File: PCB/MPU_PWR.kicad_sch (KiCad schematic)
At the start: 1 part, among them U2 STM32MP157FABx

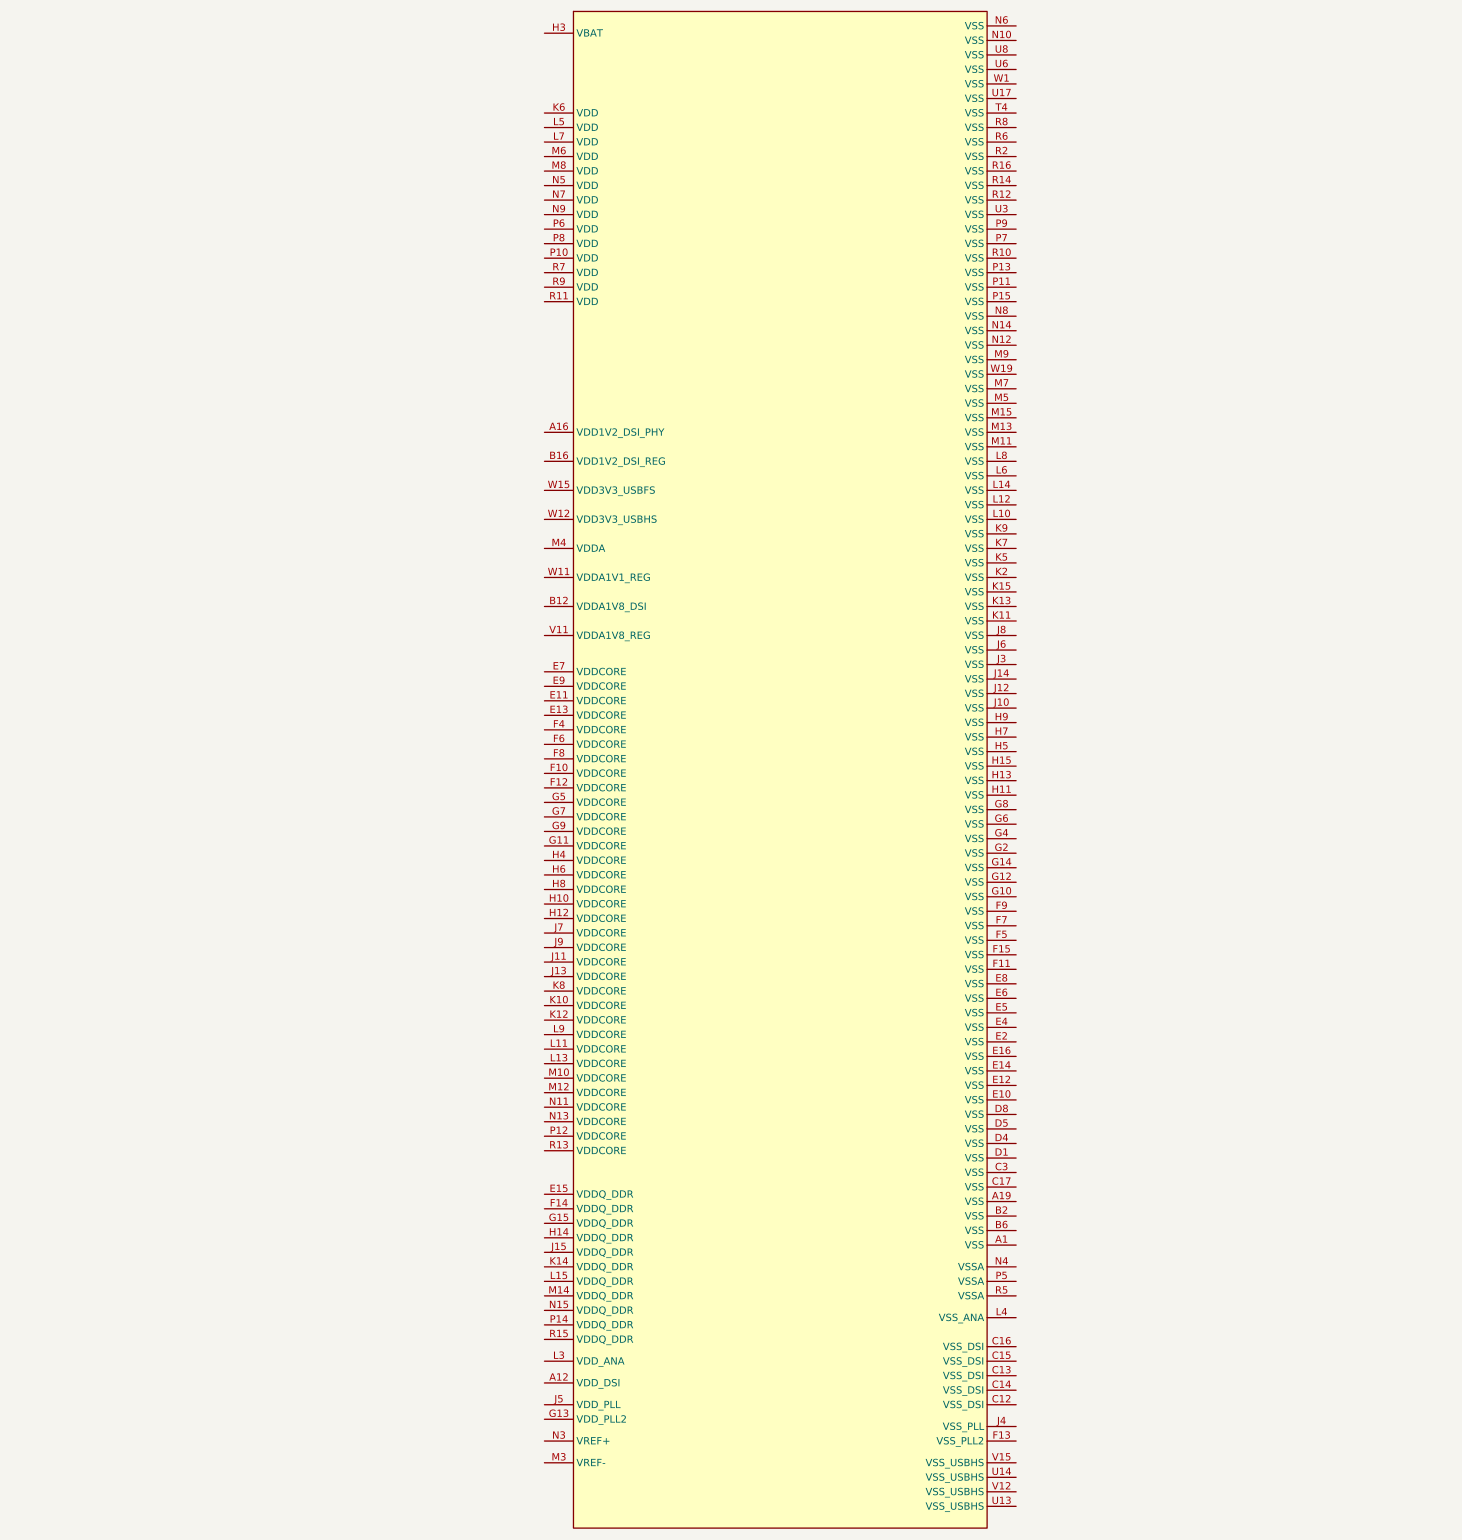
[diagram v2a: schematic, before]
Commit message: PCB_UPDATE. PWR DONE, DDR STARTED
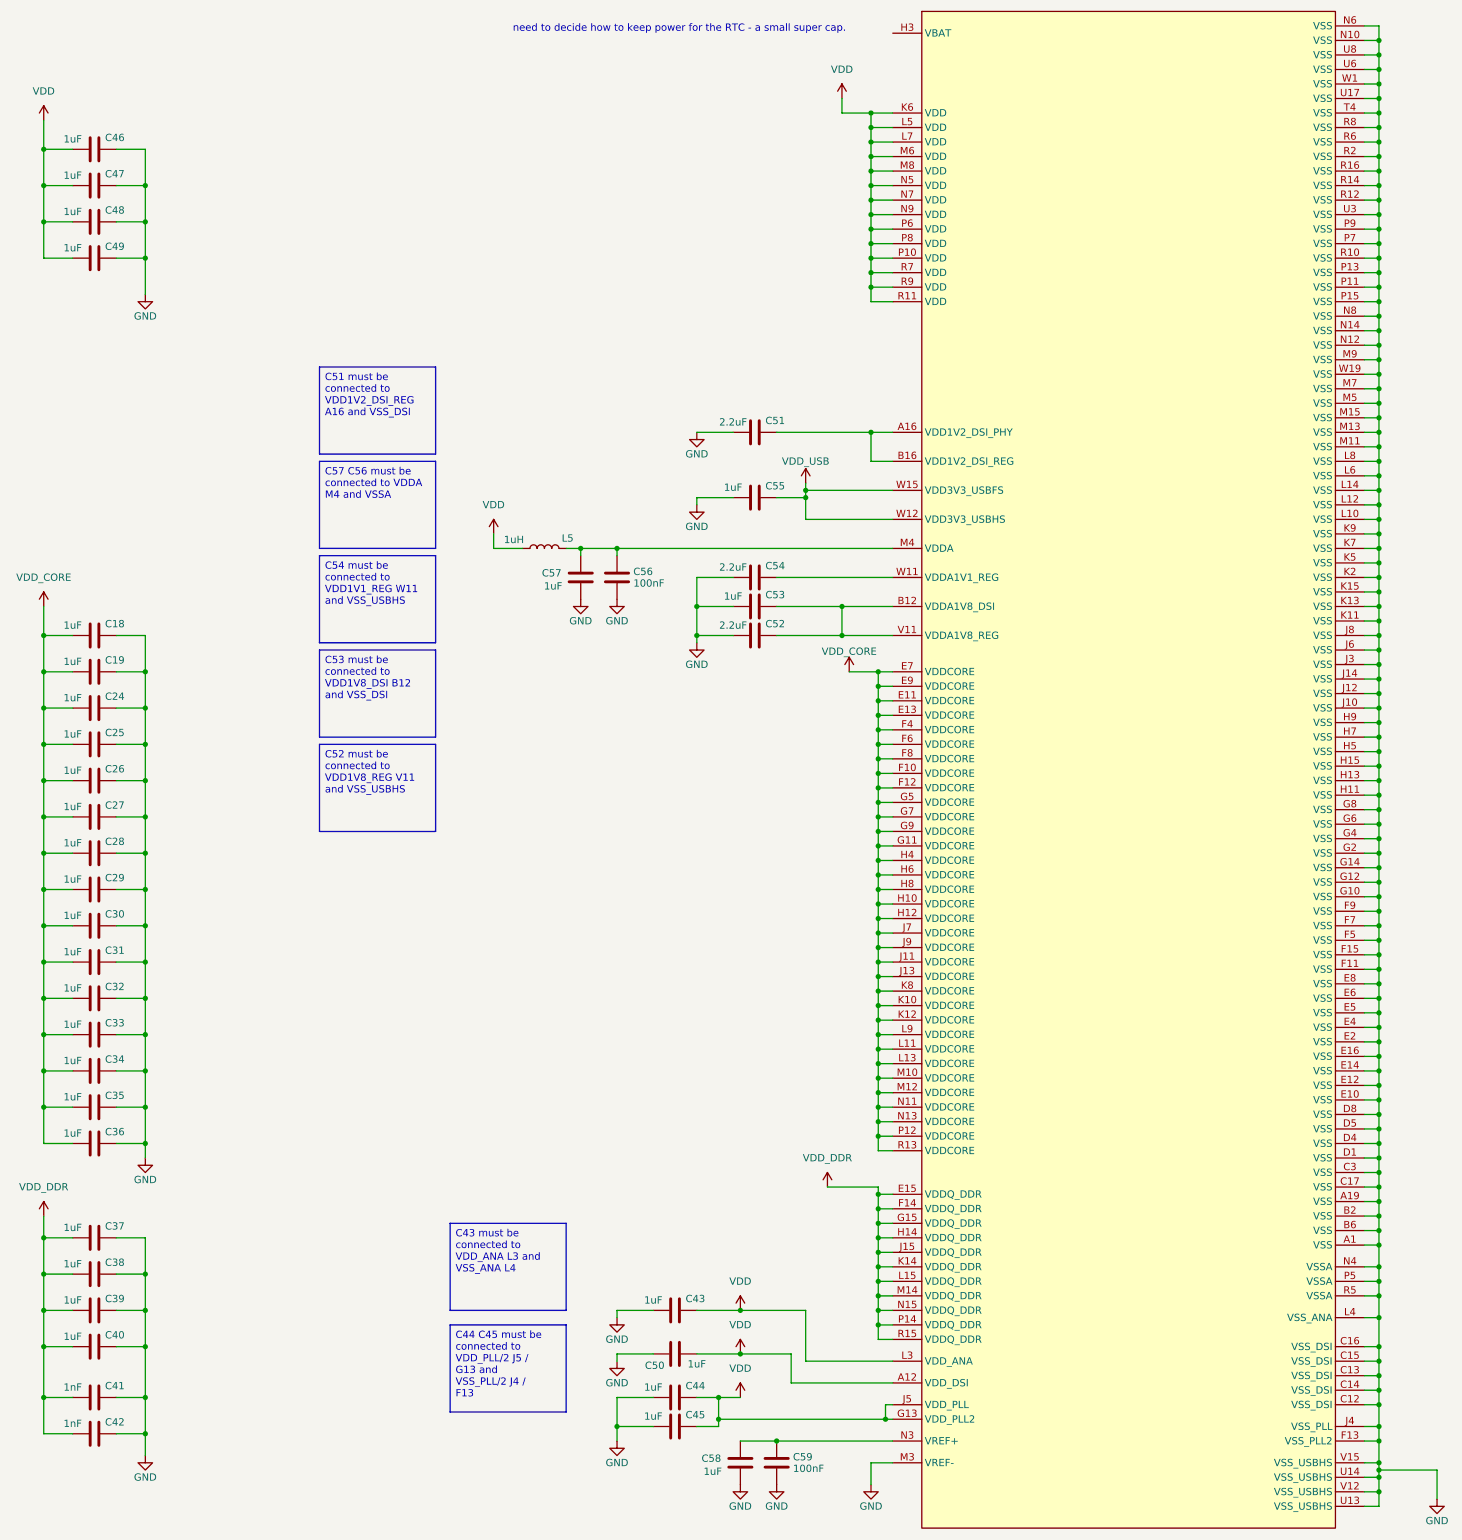
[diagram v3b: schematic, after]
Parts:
- added C18, C19, C24, C25, C26, C27, C28, C29, C30, C31, C32, C33, C34, C35, C36, C37, C38, C39, C40, C43, C44, C45, C46, C47, C48, C49, C50, C53, C55, C57, C58: 1uF, Capacitor_SMD:C_0402_1005Metric, symbol Device:C
- added C41, C42: 1nF, Capacitor_SMD:C_0402_1005Metric, symbol Device:C
- added C51, C52, C54: 2.2uF, Capacitor_SMD:C_0402_1005Metric, symbol Device:C
- added C56, C59: 100nF, Capacitor_SMD:C_0402_1005Metric, symbol Device:C
- added L5: 1uH, Inductor_SMD:L_0201_0603Metric, symbol Device:L
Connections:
- net GND: now reaches U2.A1 (VSS)
- net GND: now also U2.A19 (VSS), U2.B2 (VSS), U2.B6 (VSS), U2.C12 (VSS_DSI), U2.C13 (VSS_DSI), U2.C14 (VSS_DSI), U2.C15 (VSS_DSI), U2.C16 (VSS_DSI), U2.C17 (VSS), U2.C3 (VSS), U2.D1 (VSS), U2.D4 (VSS), U2.D5 (VSS), U2.D8 (VSS), U2.E10 (VSS), U2.E12 (VSS), U2.E14 (VSS), U2.E16 (VSS), U2.E2 (VSS), U2.E4 (VSS), U2.E5 (VSS), U2.E6 (VSS), U2.E8 (VSS), U2.F11 (VSS), U2.F13 (VSS_PLL2), U2.F15 (VSS), U2.F5 (VSS), U2.F7 (VSS), U2.F9 (VSS), U2.G10 (VSS), U2.G12 (VSS), U2.G14 (VSS), U2.G2 (VSS), U2.G4 (VSS), U2.G6 (VSS), U2.G8 (VSS), U2.H11 (VSS), U2.H13 (VSS), U2.H15 (VSS), U2.H5 (VSS), U2.H7 (VSS), U2.H9 (VSS), U2.J10 (VSS), U2.J12 (VSS), U2.J14 (VSS), U2.J3 (VSS), U2.J4 (VSS_PLL), U2.J6 (VSS), U2.J8 (VSS), U2.K11 (VSS), U2.K13 (VSS), U2.K15 (VSS), U2.K2 (VSS), U2.K5 (VSS), U2.K7 (VSS), U2.K9 (VSS), U2.L10 (VSS), U2.L12 (VSS), U2.L14 (VSS), U2.L4 (VSS_ANA), U2.L6 (VSS), U2.L8 (VSS), U2.M11 (VSS), U2.M13 (VSS), U2.M15 (VSS), U2.M3 (VREF-), U2.M5 (VSS), U2.M7 (VSS), U2.M9 (VSS), U2.N10 (VSS), U2.N12 (VSS), U2.N14 (VSS), U2.N4 (VSSA), U2.N6 (VSS), U2.N8 (VSS), U2.P11 (VSS), U2.P13 (VSS), U2.P15 (VSS), U2.P5 (VSSA), U2.P7 (VSS), U2.P9 (VSS), U2.R10 (VSS), U2.R12 (VSS), U2.R14 (VSS), U2.R16 (VSS), U2.R2 (VSS), U2.R5 (VSSA), U2.R6 (VSS), U2.R8 (VSS), U2.T4 (VSS), U2.U13 (VSS_USBHS), U2.U14 (VSS_USBHS), U2.U17 (VSS), U2.U3 (VSS), U2.U6 (VSS), U2.U8 (VSS), U2.V12 (VSS_USBHS), U2.V15 (VSS_USBHS), U2.W1 (VSS), U2.W19 (VSS), C18.1, C19.1, C24.1, C25.1, C26.1, C27.1, C28.1, C29.1, C30.1, C31.1, C32.1, C33.1, C34.1, C35.1, C36.1, C37.1, C38.1, C39.1, C40.1, C41.1, C42.1, C43.2, C44.2, C45.2, C46.1, C47.1, C48.1, C49.1, C50.1, C51.2, C52.2, C53.2, C54.2, C55.2, C56.2, C57.2, C58.2, C59.2
- net VDD: now reaches U2.A12 (VDD_DSI)
- net VDD: now also U2.G13 (VDD_PLL2), U2.J5 (VDD_PLL), U2.K6 (VDD), U2.L3 (VDD_ANA), U2.L5 (VDD), U2.L7 (VDD), U2.M6 (VDD), U2.M8 (VDD), U2.N5 (VDD), U2.N7 (VDD), U2.N9 (VDD), U2.P10 (VDD), U2.P6 (VDD), U2.P8 (VDD), U2.R11 (VDD), U2.R7 (VDD), U2.R9 (VDD), C43.1, C44.1, C45.1, C46.2, C47.2, C48.2, C49.2, C50.2, L5.1
- net at U2.A16 (VDD1V2_DSI_PHY): now also U2.B16 (VDD1V2_DSI_REG), C51.1
- net at U2.B12 (VDDA1V8_DSI): now also U2.V11 (VDDA1V8_REG), C52.1, C53.1
- net VDD_CORE: now reaches U2.E11 (VDDCORE)
- net VDD_CORE: now also U2.E13 (VDDCORE), U2.E7 (VDDCORE), U2.E9 (VDDCORE), U2.F10 (VDDCORE), U2.F12 (VDDCORE), U2.F4 (VDDCORE), U2.F6 (VDDCORE), U2.F8 (VDDCORE), U2.G11 (VDDCORE), U2.G5 (VDDCORE), U2.G7 (VDDCORE), U2.G9 (VDDCORE), U2.H10 (VDDCORE), U2.H12 (VDDCORE), U2.H4 (VDDCORE), U2.H6 (VDDCORE), U2.H8 (VDDCORE), U2.J11 (VDDCORE), U2.J13 (VDDCORE), U2.J7 (VDDCORE), U2.J9 (VDDCORE), U2.K10 (VDDCORE), U2.K12 (VDDCORE), U2.K8 (VDDCORE), U2.L11 (VDDCORE), U2.L13 (VDDCORE), U2.L9 (VDDCORE), U2.M10 (VDDCORE), U2.M12 (VDDCORE), U2.N11 (VDDCORE), U2.N13 (VDDCORE), U2.P12 (VDDCORE), U2.R13 (VDDCORE), C18.2, C19.2, C24.2, C25.2, C26.2, C27.2, C28.2, C29.2, C30.2, C31.2, C32.2, C33.2, C34.2, C35.2, C36.2
- net VDD_DDR: now reaches U2.E15 (VDDQ_DDR)
- net VDD_DDR: now also U2.F14 (VDDQ_DDR), U2.G15 (VDDQ_DDR), U2.H14 (VDDQ_DDR), U2.J15 (VDDQ_DDR), U2.K14 (VDDQ_DDR), U2.L15 (VDDQ_DDR), U2.M14 (VDDQ_DDR), U2.N15 (VDDQ_DDR), U2.P14 (VDDQ_DDR), U2.R15 (VDDQ_DDR), C37.2, C38.2, C39.2, C40.2, C41.2, C42.2
- net at U2.M4 (VDDA): now also C56.1, C57.1, L5.2
- net at U2.N3 (VREF+): now also C58.1, C59.1
- net at U2.W11 (VDDA1V1_REG): now also C54.1
- net VDD_USB: now reaches U2.W12 (VDD3V3_USBHS)
- net VDD_USB: now also U2.W15 (VDD3V3_USBFS), C55.1
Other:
- note added: "need to decide how to keep power for the RTC - a small super cap."

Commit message: PCB_UPDATE
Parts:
- added C1: CPH3225A, lib:CAPCP3225X100N, symbol CPH3225A:CPH3225A
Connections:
- net GND: now also C1.2
- net at U2.H3 (VBAT): now also C1.1
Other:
- note removed: "need to decide how to keep power for the RTC - a small super cap."
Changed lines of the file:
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@@
 	(generator_version "9.0")
 	(paper "A3")
-	(text "need to decide how to keep power for the RTC - a small super cap."
-		(exclude_from_sim no)
-		(at 134.112 20.828 0)
-		(effects
-			(font
-				(size 1.27 1.27)
-			)
-		)
-	)
 	(text_box "C43 must be connected to VDD_ANA L3 and VSS_ANA L4\n"
 		(exclude_from_sim no)
@@
 	(wire
 		(pts
+			(xy 139.7 21.59) (xy 171.45 21.59)
+		)
+		(stroke
+			(width 0)
+			(type default)
+		)
+	)
+	(wire
+		(pts
 			(xy 151.13 91.44) (xy 167.64 91.44)
 		)
@@
 	(symbol
 		(lib_id "power:GND")
+		(at 139.7 29.21 0)
+		(unit 1)
+		(exclude_from_sim no)
+		(in_bom yes)
+		(on_board yes)
+		(dnp no)
+		(property "Reference" "#PWR0162"
+			(at 139.7 35.56 0)
+			(effects
+				(font
+					(size 1.27 1.27)
+				)
+				(hide yes)
+			)
+		)
+		(property "Value" "GND"
+			(at 139.7 33.02 0)
+			(effects
+				(font
+					(size 1.27 1.27)
+				)
+			)
+		)
+		(property "Footprint" ""
+			(at 139.7 29.21 0)
+			(effects
+				(font
+					(size 1.27 1.27)
+				)
+				(hide yes)
+			)
+		)
+		(property "Datasheet" ""
+			(at 139.7 29.21 0)
+			(effects
+				(font
+					(size 1.27 1.27)
+				)
+				(hide yes)
+			)
+		)
+		(property "Description" "Power symbol creates a global label with name \"GND\" , ground"
+			(at 139.7 29.21 0)
+			(effects
+				(font
+					(size 1.27 1.27)
+				)
+				(hide yes)
+			)
+		)
+		(pin "1"
+		)
+		(instances
+			(project "MPU_MOD"
+				(path "/65890f61-d586-475b-928a-b635a5e4e59e/f922126e-a4bd-4f88-a222-a0ba90de18ce"
+					(reference "#PWR0162")
+					(unit 1)
+				)
+			)
+		)
+	)
+	(symbol
+		(lib_id "power:GND")
 		(at 123.19 120.65 0)
 		(unit 1)
@@
 		)
 		(instances
-			(project "MPU_MOD"
+			(project ""
+				(path "/65890f61-d586-475b-928a-b635a5e4e59e/9899e005-10ba-4bf4-b936-8d0d8a1813b9"
+					(reference "U2")
+					(unit 1)
+				)
 				(path "/65890f61-d586-475b-928a-b635a5e4e59e/f922126e-a4bd-4f88-a222-a0ba90de18ce"
 					(reference "U2")
@@
 					(unit 1)
 				)
+			)
+		)
+	)
+	(symbol
+		(lib_id "CPH3225A:CPH3225A")
+		(at 139.7 26.67 90)
+		(unit 1)
+		(exclude_from_sim no)
+		(in_bom yes)
+		(on_board yes)
+		(dnp no)
+		(fields_autoplaced yes)
+		(property "Reference" "C1"
+			(at 143.51 24.1299 90)
+			(effects
+				(font
+					(size 1.27 1.27)
+				)
+				(justify right)
+			)
+		)
+		(property "Value" "CPH3225A"
+			(at 143.51 26.6699 90)
+			(effects
+				(font
+					(size 1.27 1.27)
+				)
+				(justify right)
+			)
+		)
+		(property "Footprint" "lib:CAPCP3225X100N"
+			(at 139.7 26.67 0)
+			(effects
+				(font
+					(size 1.27 1.27)
+				)
+				(justify bottom)
+				(hide yes)
+			)
+		)
+		(property "Datasheet" ""
+			(at 139.7 26.67 0)
+			(effects
+				(font
+					(size 1.27 1.27)
+				)
+				(hide yes)
+			)
+		)
+		(property "Description" ""
+			(at 139.7 26.67 0)
+			(effects
+				(font
+					(size 1.27 1.27)
+				)
+				(hide yes)
+			)
+		)
+		(property "MF" "Seiko Instruments"
+			(at 139.7 26.67 0)
+			(effects
+				(font
+					(size 1.27 1.27)
+				)
+				(justify bottom)
+				(hide yes)
+			)
+		)
+		(property "Description_1" "11 mF (EDLC) Supercapacitor 3.3 V 1210 (3225 Metric) - -"
+			(at 139.7 26.67 0)
+			(effects
+				(font
+					(size 1.27 1.27)
+				)
+				(justify bottom)
+				(hide yes)
+			)
+		)
+		(property "Package" "1210 Seiko"
+			(at 139.7 26.67 0)
+			(effects
+				(font
+					(size 1.27 1.27)
+				)
+				(justify bottom)
+				(hide yes)
+			)
+		)
+		(property "Price" "None"
+			(at 139.7 26.67 0)
+			(effects
+				(font
+					(size 1.27 1.27)
+				)
+				(justify bottom)
+				(hide yes)
+			)
+		)
+		(property "SnapEDA_Link" "https://www.snapeda.com/parts/CPH3225A/Seiko/view-part/?ref=snap"
+			(at 139.7 26.67 0)
+			(effects
+				(font
+					(size 1.27 1.27)
+				)
+				(justify bottom)
+				(hide yes)
+			)
+		)
+		(property "MP" "CPH3225A"
+			(at 139.7 26.67 0)
+			(effects
+				(font
+					(size 1.27 1.27)
+				)
+				(justify bottom)
+				(hide yes)
+			)
+		)
+		(property "Availability" "In Stock"
+			(at 139.7 26.67 0)
+			(effects
+				(font
+					(size 1.27 1.27)
+				)
+				(justify bottom)
+				(hide yes)
+			)
+		)
+		(property "Check_prices" "https://www.snapeda.com/parts/CPH3225A/Seiko/view-part/?ref=eda"
+			(at 139.7 26.67 0)
+			(effects
+				(font
+					(size 1.27 1.27)
+				)
+				(justify bottom)
+				(hide yes)
+			)
+		)
+		(pin "2"
+		)
+		(pin "1"
+		)
+		(instances
+			(project ""
+				(path "/65890f61-d586-475b-928a-b635a5e4e59e/f922126e-a4bd-4f88-a222-a0ba90de18ce"
+					(reference "C1")
+					(unit 1)
+				)

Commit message: PCB_UPDATE
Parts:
- renumbered C46 to C301, C47 to C302, C48 to C303, C49 to C304, C18 to C305, C19 to C306, C24 to C307, C25 to C308, C26 to C309, C27 to C310, C28 to C311, C29 to C312, C30 to C313, C31 to C314, C32 to C315, C33 to C316, C34 to C317, C35 to C318, C36 to C319, C37 to C320, C38 to C321, C39 to C322, C40 to C323, C41 to C324, C42 to C325, C57 to C326, C56 to C327, C43 to C328, C50 to C329, C44 to C330, C45 to C331, C1 to C332, C58 to C333, C51 to C334, C55 to C335, C54 to C336, C53 to C337, C52 to C338, C59 to C339, L5 to L301, U2 to U301

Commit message: PCB_UPDATE
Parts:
- L301: footprint Inductor_SMD:L_0201_0603Metric -> Inductor_SMD:L_0603_1608Metric
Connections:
- net VDDA: now reaches C326.1, C327.1, L301.2, U301.M4 (VDDA)
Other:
- moved on the sheet: C326, C327
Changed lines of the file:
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@@
 	)
 	(junction
+		(at 121.92 111.76)
+		(diameter 0)
+		(color 0 0 0 0)
+	)
+	(junction
 		(at 40.64 177.8)
 		(diameter 0)
@@
 	)
 	(junction
+		(at 128.27 111.76)
+		(diameter 0)
+		(color 0 0 0 0)
+	)
+	(junction
 		(at 256.54 27.94)
 		(diameter 0)
@@
 	)
 	(junction
-		(at 123.19 111.76)
-		(diameter 0)
-		(color 0 0 0 0)
-	)
-	(junction
 		(at 140.97 260.35)
 		(diameter 0)
@@
 	)
 	(junction
-		(at 116.84 111.76)
-		(diameter 0)
-		(color 0 0 0 0)
-	)
-	(junction
 		(at 40.64 251.46)
 		(diameter 0)
@@
 	(wire
 		(pts
-			(xy 116.84 111.76) (xy 116.84 113.03)
+			(xy 121.92 111.76) (xy 121.92 113.03)
 		)
 		(stroke
@@
 	(wire
 		(pts
-			(xy 114.3 111.76) (xy 116.84 111.76)
+			(xy 114.3 111.76) (xy 121.92 111.76)
 		)
 		(stroke
@@
 	(wire
 		(pts
-			(xy 123.19 111.76) (xy 123.19 113.03)
+			(xy 128.27 111.76) (xy 128.27 113.03)
 		)
 		(stroke
@@
 	(wire
 		(pts
-			(xy 171.45 111.76) (xy 123.19 111.76)
+			(xy 171.45 111.76) (xy 128.27 111.76)
 		)
 		(stroke
@@
 	(wire
 		(pts
-			(xy 123.19 111.76) (xy 116.84 111.76)
+			(xy 121.92 111.76) (xy 128.27 111.76)
 		)
 		(stroke
@@
 		)
 	)
+	(label "VDDA"
+		(at 115.57 111.76 0)
+		(effects
+			(font
+				(size 1.27 1.27)
+			)
+			(justify left bottom)
+		)
+	)
 	(symbol
 		(lib_id "Device:C")
@@
 	(symbol
 		(lib_id "power:GND")
-		(at 123.19 120.65 0)
+		(at 128.27 120.65 0)
 		(unit 1)
 		(exclude_from_sim no)
@@
 		(dnp no)
 		(property "Reference" "#PWR0309"
-			(at 123.19 127 0)
+			(at 128.27 127 0)
 			(effects
 				(font
@@
 		)
 		(property "Value" "GND"
-			(at 123.19 124.46 0)
+			(at 128.27 124.46 0)
 			(effects
 				(font
@@
 		)
 		(property "Footprint" ""
-			(at 123.19 120.65 0)
+			(at 128.27 120.65 0)
 			(effects
 				(font
@@
 		)
 		(property "Datasheet" ""
-			(at 123.19 120.65 0)
+			(at 128.27 120.65 0)
 			(effects
 				(font
@@
 		)
 		(property "Description" "Power symbol creates a global label with name \"GND\" , ground"
-			(at 123.19 120.65 0)
+			(at 128.27 120.65 0)
 			(effects
 				(font
@@
 	(symbol
 		(lib_id "power:GND")
-		(at 116.84 120.65 0)
+		(at 121.92 120.65 0)
 		(unit 1)
 		(exclude_from_sim no)
@@
 		(dnp no)
 		(property "Reference" "#PWR0308"
-			(at 116.84 127 0)
+			(at 121.92 127 0)
 			(effects
 				(font
@@
 		)
 		(property "Value" "GND"
-			(at 116.84 124.46 0)
+			(at 121.92 124.46 0)
 			(effects
 				(font
@@
 		)
 		(property "Footprint" ""
-			(at 116.84 120.65 0)
+			(at 121.92 120.65 0)
 			(effects
 				(font
@@
 		)
 		(property "Datasheet" ""
-			(at 116.84 120.65 0)
+			(at 121.92 120.65 0)
 			(effects
 				(font
@@
 		)
 		(property "Description" "Power symbol creates a global label with name \"GND\" , ground"
-			(at 116.84 120.65 0)
+			(at 121.92 120.65 0)
 			(effects
 				(font
@@
 	(symbol
 		(lib_id "Device:C")
-		(at 123.19 116.84 0)
+		(at 128.27 116.84 0)
 		(unit 1)
 		(exclude_from_sim no)
@@
 		(dnp no)
 		(property "Reference" "C327"
-			(at 127.762 115.824 0)
+			(at 132.842 115.824 0)
 			(effects
 				(font
@@
 		)
 		(property "Value" "100nF"
-			(at 128.778 117.856 0)
+			(at 133.858 117.856 0)
 			(effects
 				(font
@@
 		)
 		(property "Footprint" "Capacitor_SMD:C_0402_1005Metric"
-			(at 124.1552 120.65 0)
+			(at 129.2352 120.65 0)
 			(effects
 				(font
@@
 		)
 		(property "Datasheet" "~"
-			(at 123.19 116.84 0)
+			(at 128.27 116.84 0)
 			(effects
 				(font
@@
 		)
 		(property "Description" "Unpolarized capacitor"
-			(at 123.19 116.84 0)
+			(at 128.27 116.84 0)
 			(effects
 				(font
@@
 		)
 		(property "P/N" " GRM155R61E104KA87J"
-			(at 123.19 116.84 0)
+			(at 128.27 116.84 0)
 			(effects
 				(font
@@
 		)
 		(property "Mouser P/N" "81-GRM155R61E104KA7J"
-			(at 123.19 116.84 0)
+			(at 128.27 116.84 0)
 			(effects
 				(font
@@
 	(symbol
 		(lib_id "Device:C")
-		(at 116.84 116.84 0)
+		(at 121.92 116.84 0)
 		(unit 1)
 		(exclude_from_sim no)
@@
 		(dnp no)
 		(property "Reference" "C326"
-			(at 111.76 116.078 0)
+			(at 116.84 116.078 0)
 			(effects
 				(font
@@
 		)
 		(property "Value" "1uF"
-			(at 112.014 118.364 0)
+			(at 117.094 118.364 0)
 			(effects
 				(font
@@
 		)
 		(property "Footprint" "Capacitor_SMD:C_0402_1005Metric"
-			(at 117.8052 120.65 0)
+			(at 122.8852 120.65 0)
 			(effects
 				(font
@@
 		)
 		(property "Datasheet" "~"
-			(at 116.84 116.84 0)
+			(at 121.92 116.84 0)
 			(effects
 				(font
@@
 		)
 		(property "Description" "Unpolarized capacitor"
-			(at 116.84 116.84 0)
+			(at 121.92 116.84 0)
 			(effects
 				(font
@@
 		)
 		(property "P/N" "GRM155R61E105KA12D"
-			(at 116.84 116.84 0)
+			(at 121.92 116.84 0)
 			(effects
 				(font
@@
 		)
 		(property "Mouser P/N" "81-GRM155R61E105KA2D"
-			(at 116.84 116.84 0)
+			(at 121.92 116.84 0)
 			(effects
 				(font
@@
 		(dnp no)
 		(property "Reference" "L301"
-			(at 114.554 109.982 90)
+			(at 111.506 109.474 90)
 			(effects
 				(font
@@
 			)
 		)
-		(property "Footprint" "Inductor_SMD:L_0201_0603Metric"
+		(property "Footprint" "Inductor_SMD:L_0603_1608Metric"
 			(at 110.49 111.76 0)
 			(effects
